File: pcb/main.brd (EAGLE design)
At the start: 100 x 100 mm, 32 parts, among them IC1 74HCT04N, IC2 74HCT04N, IC3 74HCT04N, IC4 74HCT04N

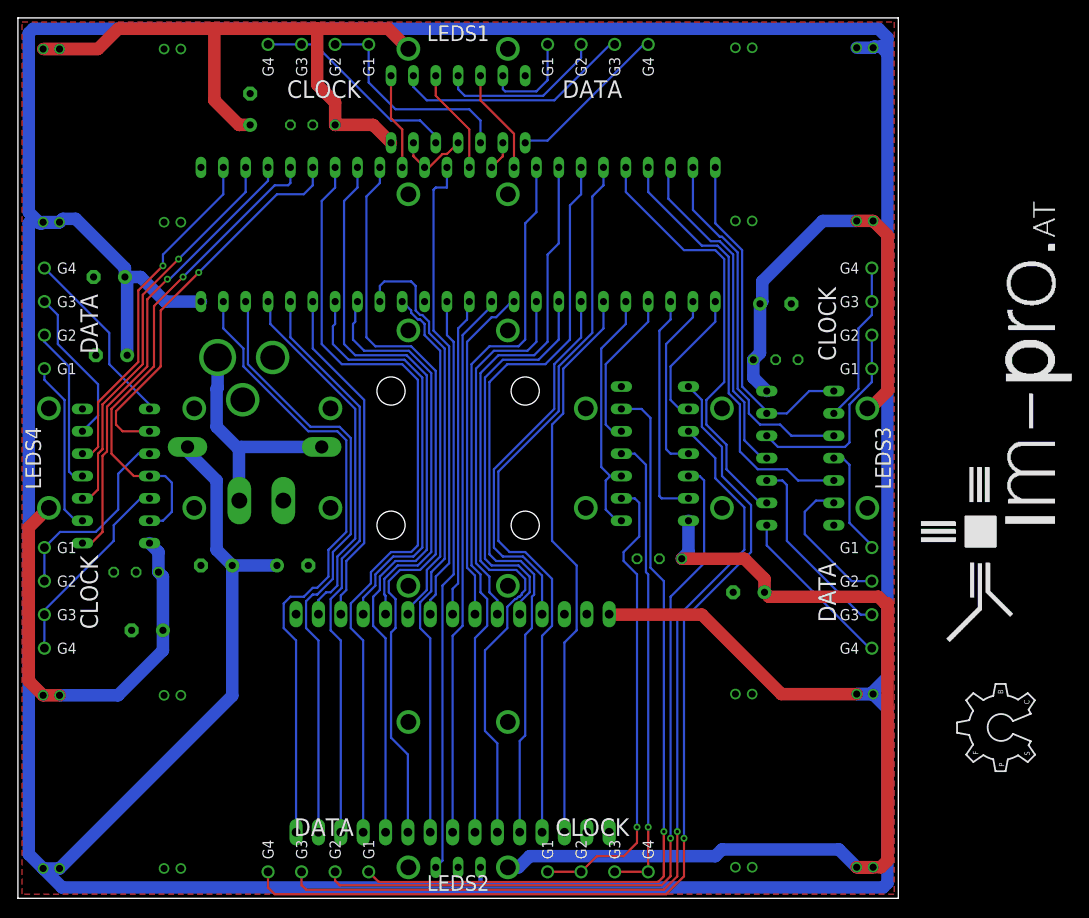
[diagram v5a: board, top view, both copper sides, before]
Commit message: finished main pcb layout
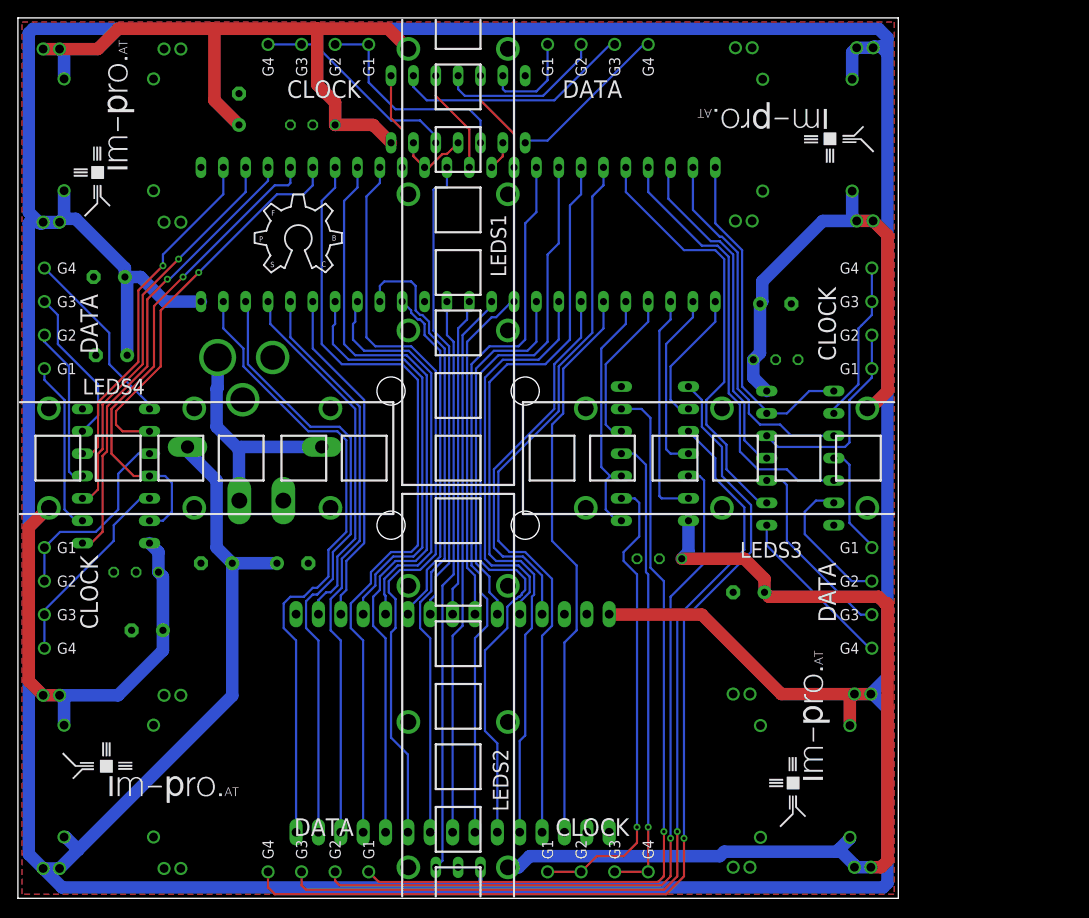
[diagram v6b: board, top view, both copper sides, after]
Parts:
- added ESP: ESP32DEVKITV1, ESP32-DEVKITV1:ESP32-DEVKITV1
- added U$3, U$4: LOGO20MM, im-pro-logo:LOGO_20MM
- U$1: value LOGO50MM -> LOGO20MM; device im-pro-logo:LOGO_50MM -> im-pro-logo:LOGO_20MM
- U$2: value ESP32DEVKITV1 -> LOGO20MM; device ESP32-DEVKITV1:ESP32-DEVKITV1 -> im-pro-logo:LOGO_20MM
- moved U$1 117.3 mm to (-45.0, -39.6), turned to 0 degrees
- moved LOGO1 105.2 mm to (-23.1, 21.1), turned to 0 degrees
- moved U$2 50.1 mm to (42.7, -41.9), flipped to the top, turned to 90 degrees
- moved C4 1.27 mm to (-24.9, 39.6)
- moved C3 0.25 mm to (-27.4, -11.9)
- moved C6 0.25 mm to (-18.8, -11.9)
- moved DCDC2 0.25 mm to (31.2, -26.2)
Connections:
- net +12V: now also DCDC1.VIN3, DCDC2.VIN3, DCDC3.VIN3, DCDC4.VIN3, ESP.30; no longer U$2.30
- net +5V/1: now also DCDC1.VOUT3
- net +5V/2: now also DCDC2.VOUT3
- net +5V/3: now also DCDC3.VOUT3
- net +5V/4: now also DCDC4.VOUT3
- net GND: now also DCDC1.GND5, DCDC1.GND6, DCDC2.GND5, DCDC2.GND6, DCDC3.GND5, DCDC3.GND6, DCDC4.GND5, DCDC4.GND6, ESP.2, ESP.29; no longer U$2.2, U$2.29
- net IO1: now also ESP.13; no longer U$2.13
- net IO12: now also ESP.27; no longer U$2.27
- net IO14: now also ESP.26; no longer U$2.26
- net IO15: now also ESP.3; no longer U$2.3
- net IO16: now also ESP.6; no longer U$2.6
- net IO17: now also ESP.7; no longer U$2.7
- net IO18: now also ESP.9; no longer U$2.9
- net IO19: now also ESP.10; no longer U$2.10
- net IO2: now also ESP.4; no longer U$2.4
- net IO21: now also ESP.11; no longer U$2.11
- net IO22: now also ESP.14; no longer U$2.14
- net IO23: now also ESP.15; no longer U$2.15
- net IO25: now also ESP.23; no longer U$2.23
- net IO26: now also ESP.24; no longer U$2.24
- net IO27: now also ESP.25; no longer U$2.25
- net IO3: now also ESP.12; no longer U$2.12
- net IO32: now also ESP.21; no longer U$2.21
- net IO33: now also ESP.22; no longer U$2.22
- net IO34: now also ESP.19; no longer U$2.19
- net IO35: now also ESP.20; no longer U$2.20
- net IO36: now also ESP.17; no longer U$2.17
- net IO39: now also ESP.18; no longer U$2.18
- net IO4: now also ESP.5; no longer U$2.5
- net IO5: now also ESP.8; no longer U$2.8
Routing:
- net +12V: track 532.9 -> 544.6 mm
- net +5V/4: track 51.5 -> 55.1 mm
- net +5V/3: track 52.0 -> 55.6 mm
- net +5V/1: track 75.8 -> 78.1 mm

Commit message: layout finished
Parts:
- C1, C10, C11, C3, C4, C6, C7, C9: value (none) -> 220u
- C12, C2, C5, C8: value (none) -> 100n
- moved U$3 19.0 mm to (-42.4, 45.5), turned to 270 degrees
